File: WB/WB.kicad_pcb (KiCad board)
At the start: 2 copper layers, 140.3 x 89.7 mm, 47 parts, among them J1 Conn_01x04, J2 Conn_01x04, J3 Conn_01x04, J4 Conn_01x04, J5 Pump, J6 Actuator, J7 Actuator, J8 Screw_Terminal_01x02, M1 Fan, Q1 Q_NMOS_GDS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

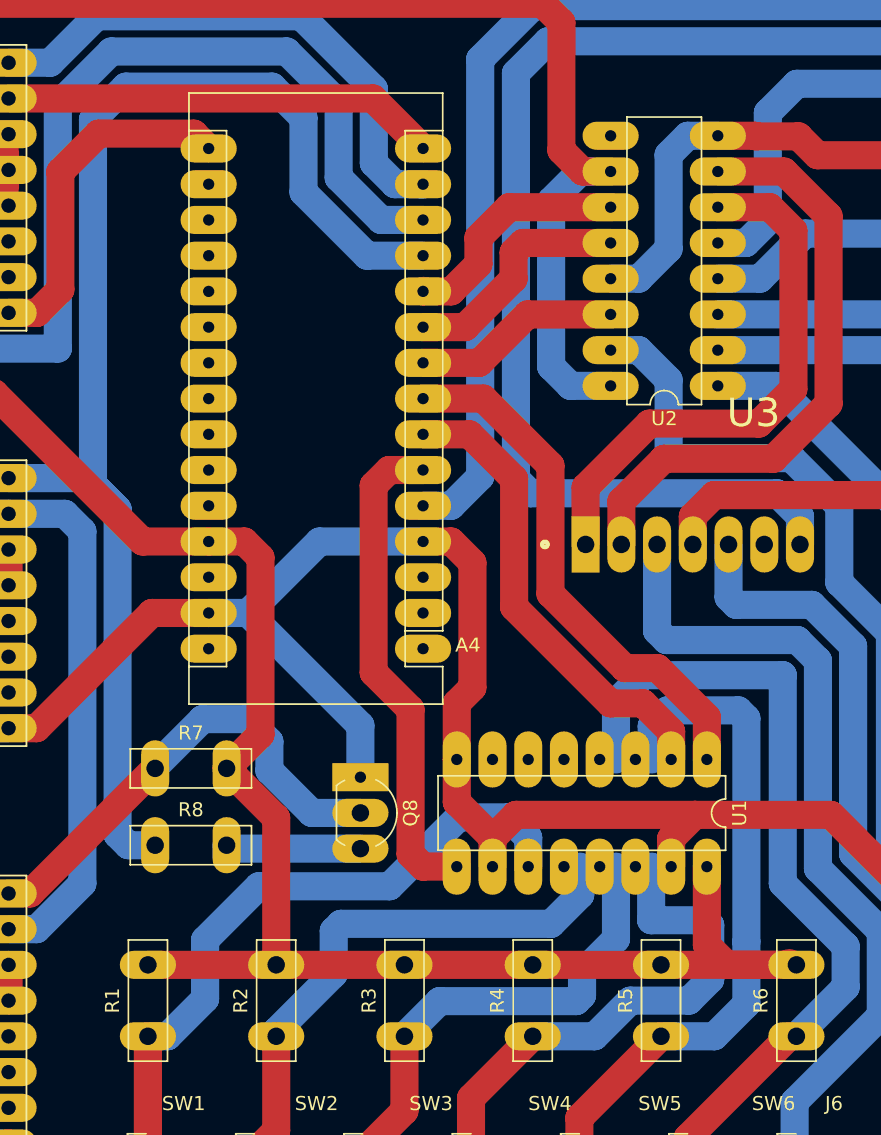
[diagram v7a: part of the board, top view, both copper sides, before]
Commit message: メインマイコンの変更
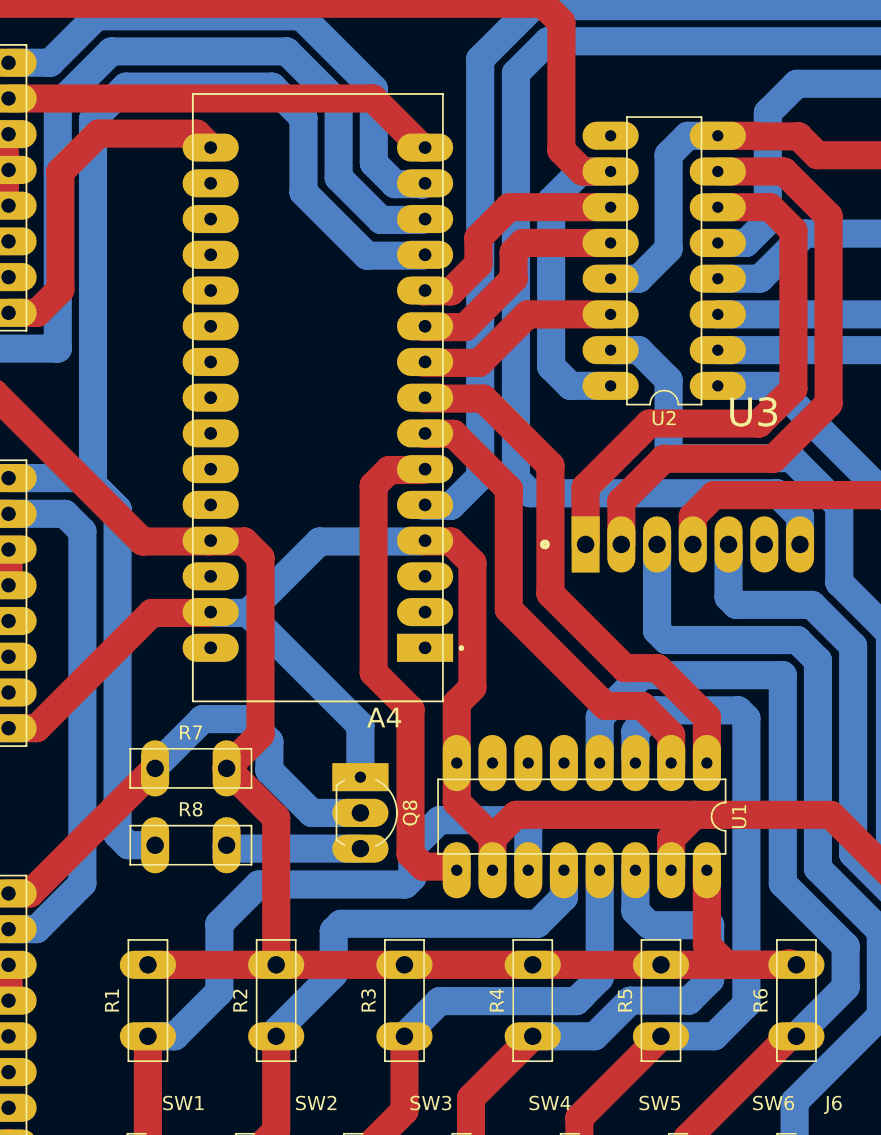
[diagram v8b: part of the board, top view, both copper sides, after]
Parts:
- A4: value Arduino_Nano_v2.x -> Arduino_Micro; footprint Module:Arduino_Nano -> ARDUINO_NANO:SHIELD_ARDUINO_NANO
- moved A4 19.3 mm to (147.8, 81.6)
- moved U1 0.25 mm to (175.5, 107.6)
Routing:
- net D0: track 46.9 -> 50.1 mm
- net D1: track 38.7 -> 37.6 mm
- net D4: track 47.8 -> 48.7 mm
- net D3: track 36.4 -> 37.1 mm
- net D5: track 56.9 -> 57.5 mm
